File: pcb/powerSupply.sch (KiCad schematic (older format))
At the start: 14 parts, among them K1 G5LE-1, U2 AZ1117-5.0, U3 AZ1117-3.3, U4 AZ1117-5.0

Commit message: first version of the new feature set
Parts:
- removed C12: 10u, Capacitor_SMD:C_0805_2012Metric_Pad1.15x1.40mm_HandSolder, symbol Device:C
- removed C16: 22u, Capacitor_SMD:C_0805_2012Metric_Pad1.15x1.40mm_HandSolder, symbol Device:C
- removed C5: 2200u, Capacitor_THT:CP_Radial_D14.0mm_P5.00mm, symbol Device:CP
- removed K1: G5LE-1, Relay_THT:Relay_SPDT_Omron-G5LE-1, symbol Relay:G5LE-1
- removed U2, U4: AZ1117-5.0, Package_TO_SOT_SMD:SOT-223-3_TabPin2, symbol Regulator_Linear:AZ1117-5.0
- added C6: 560u, Capacitor_SMD:CP_Elec_10x10.5, symbol Device:CP
- added C7: 10u, Capacitor_SMD:C_0805_2012Metric, symbol Device:C
- added D5, D6: LED/red, Capacitor_SMD:C_0805_2012Metric, symbol Device:LED
- added D8: SD0805S020S1R0, Diode_SMD:D_0805_2012Metric, symbol Device:D
- added D9: LED/green, Capacitor_SMD:C_0805_2012Metric, symbol Device:LED
- added F1: 12A/slow, ICs_own:Fuse_1206_3216Metric, symbol Device:Fuse
- added K1: CP1SA-12V-Z, Relay_own:CP1SA12VZ, symbol Relay_own:CP1SA-12V-Z
- added PS1: V78E05-1000-SMT-TR, ICs_own:SOP254P1140X825-10N, symbol Regulator_Switching_own:V78E05-1000-SMT-TR
- added R14: 2.4k, Resistor_SMD:R_0805_2012Metric, symbol Device:R
- added R17: 620, Resistor_SMD:R_0805_2012Metric, symbol Device:R
- C10: renamed from C6; footprint Capacitor_SMD:C_0805_2012Metric_Pad1.15x1.40mm_HandSolder -> Capacitor_SMD:C_0805_2012Metric
- C11: renamed from C7; footprint Capacitor_SMD:C_0805_2012Metric_Pad1.15x1.40mm_HandSolder -> Capacitor_SMD:C_0805_2012Metric
- C8: value 10u -> 100n; footprint Capacitor_SMD:C_0805_2012Metric_Pad1.15x1.40mm_HandSolder -> Capacitor_SMD:C_0805_2012Metric
- C9: footprint Capacitor_SMD:C_0805_2012Metric_Pad1.15x1.40mm_HandSolder -> Capacitor_SMD:C_0805_2012Metric
- D7: renamed from D3; footprint Diode_SMD:D_0805_2012Metric_Pad1.15x1.40mm_HandSolder -> Diode_SMD:D_0805_2012Metric
- R15: renamed from R22; footprint Resistor_SMD:R_0805_2012Metric_Pad1.15x1.40mm_HandSolder -> Resistor_SMD:R_0805_2012Metric
- R16: renamed from R6; footprint Resistor_SMD:R_0805_2012Metric_Pad1.15x1.40mm_HandSolder -> Resistor_SMD:R_0805_2012Metric
- renumbered U3 to U2
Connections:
- wire segments 52 -> 59
- no-connect marks 1 -> 0
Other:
- moved on the sheet: D7, R15, R16

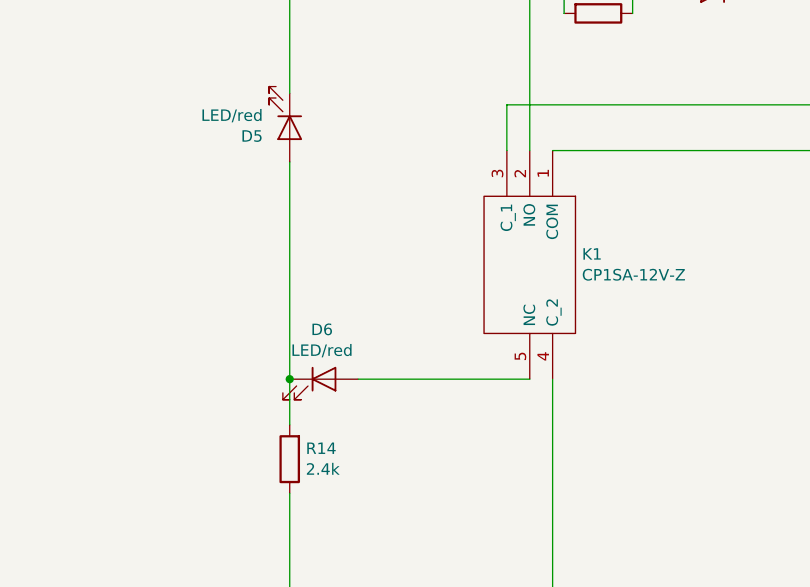
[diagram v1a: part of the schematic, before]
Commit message: removed the relais-error led
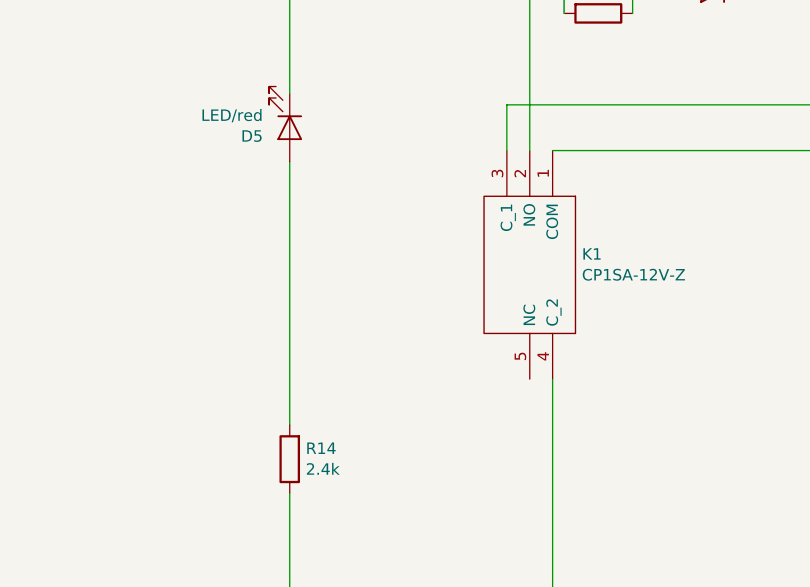
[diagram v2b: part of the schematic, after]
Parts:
- removed D6: LED/red, Capacitor_SMD:C_0805_2012Metric, symbol Device:LED
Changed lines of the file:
@@
-$EndComp
-$Comp
-L Device:LED D6
-U 1 1 5C98DA28
-P 1950 2700
-F 0 "D6" H 1941 2916 50  0000 C CNN
-F 1 "LED/red" H 1941 2825 50  0000 C CNN
-F 2 "Capacitor_SMD:C_0805_2012Metric" H 1950 2700 50  0001 C CNN
-F 3 "~" H 1950 2700 50  0001 C CNN
-	1    1950 2700
-	1    0    0    -1
 $EndComp
 $Comp
@@
 Wire Wire Line
 	1800 1450 1800 1000
-Wire Wire Line
-	2100 2700 2850 2700
-Wire Wire Line
-	1800 2700 1800 2900
 $Comp
 L Regulator_Switching_own:V78E05-1000-SMT-TR PS1
@@
 Wire Wire Line
 	1800 4650 2950 4650
-Connection ~ 1800 2700
-Wire Wire Line
-	1800 1750 1800 2700
 Wire Wire Line
 	8400 4650 9150 4650
@@
 Wire Wire Line
 	10200 4650 10600 4650
+Wire Wire Line
+	1800 1750 1800 2900
 $EndSCHEMATC

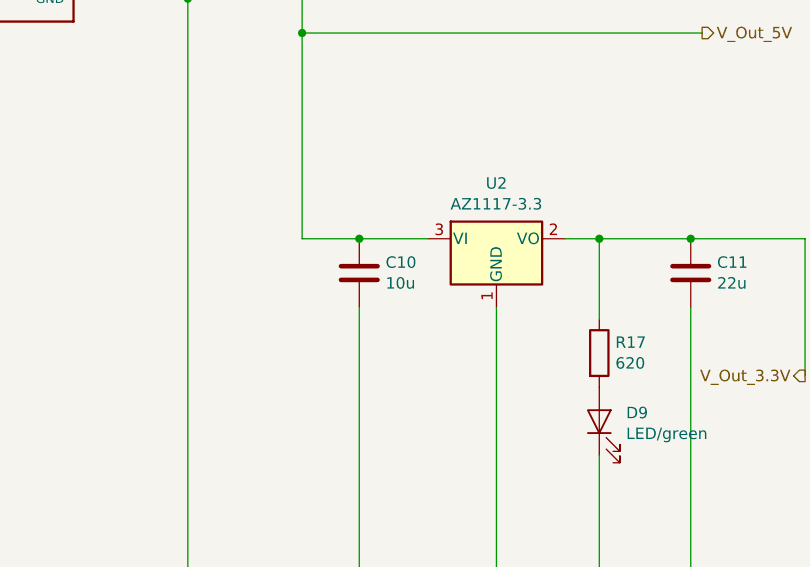
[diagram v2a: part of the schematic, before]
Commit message: Changed a capacitor in the power supply (10u to 22u) for more capacity/stability
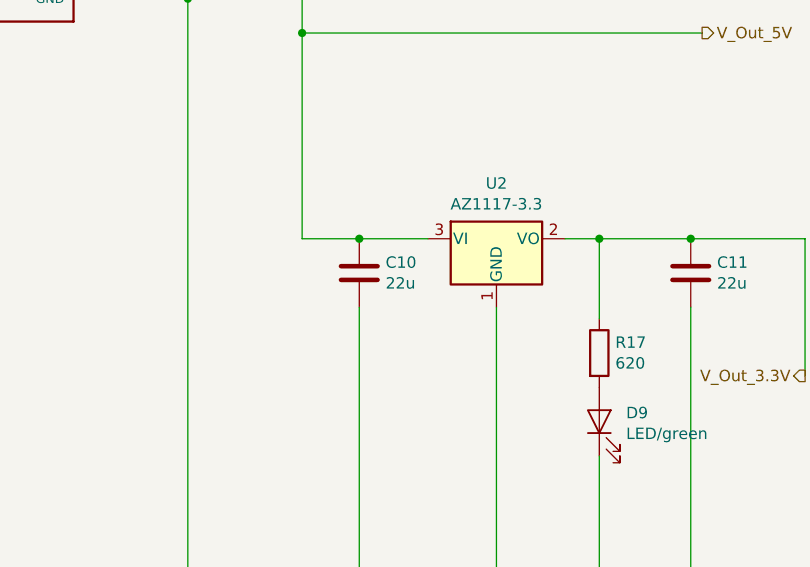
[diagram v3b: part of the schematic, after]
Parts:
- C10: value 10u -> 22u
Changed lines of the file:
@@
 P 9150 3200
 F 0 "C10" H 9265 3246 50  0000 L CNN
-F 1 "10u" H 9265 3155 50  0000 L CNN
+F 1 "22u" H 9265 3155 50  0000 L CNN
 F 2 "Capacitor_SMD:C_0805_2012Metric" H 9188 3050 50  0001 C CNN
 F 3 "~" H 9150 3200 50  0001 C CNN
